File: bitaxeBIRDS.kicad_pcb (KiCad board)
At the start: 6 copper layers, 65 x 112 mm, 219 parts, among them J1 XT30, J2 USB_C_Receptacle_USB2.0, J3 Conn_01x04, J4 Conn_01x04, SW1 SWITCH-SPST, SW2 SWITCH-SPST, U1 TPSM861253RDXR, U10 MCP1824T-1202E/OT, U11 MCP1824T-1202E/OT, U12 MCP1824T-1202E/OT, U13 EMC2103-2, U2 TPS546D24S, U3 TPS546D24S, U4 W25Q16JVUXIQ TR, U5 TPS22919DCKR, U6 RP2040, U7 SK6812, U8 SN74AVC4T774, U9 MCP1824T-1202E/OT, Y1 12MHz, Y2 50MHz

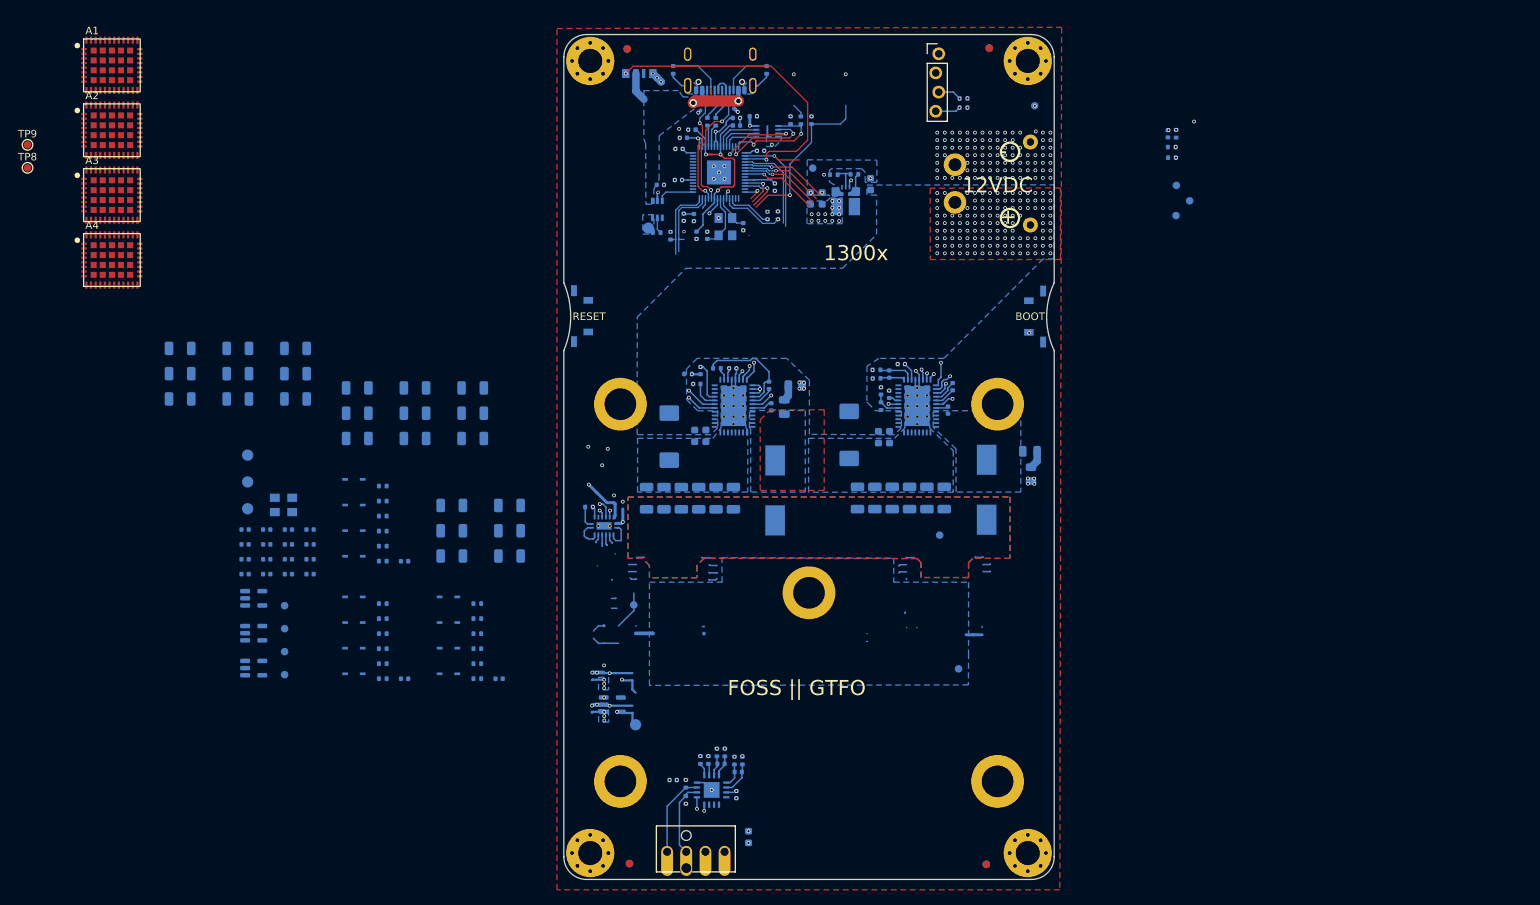
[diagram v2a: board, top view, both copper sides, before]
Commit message: switched to smaller level shifter diodes. switched ASIC modes
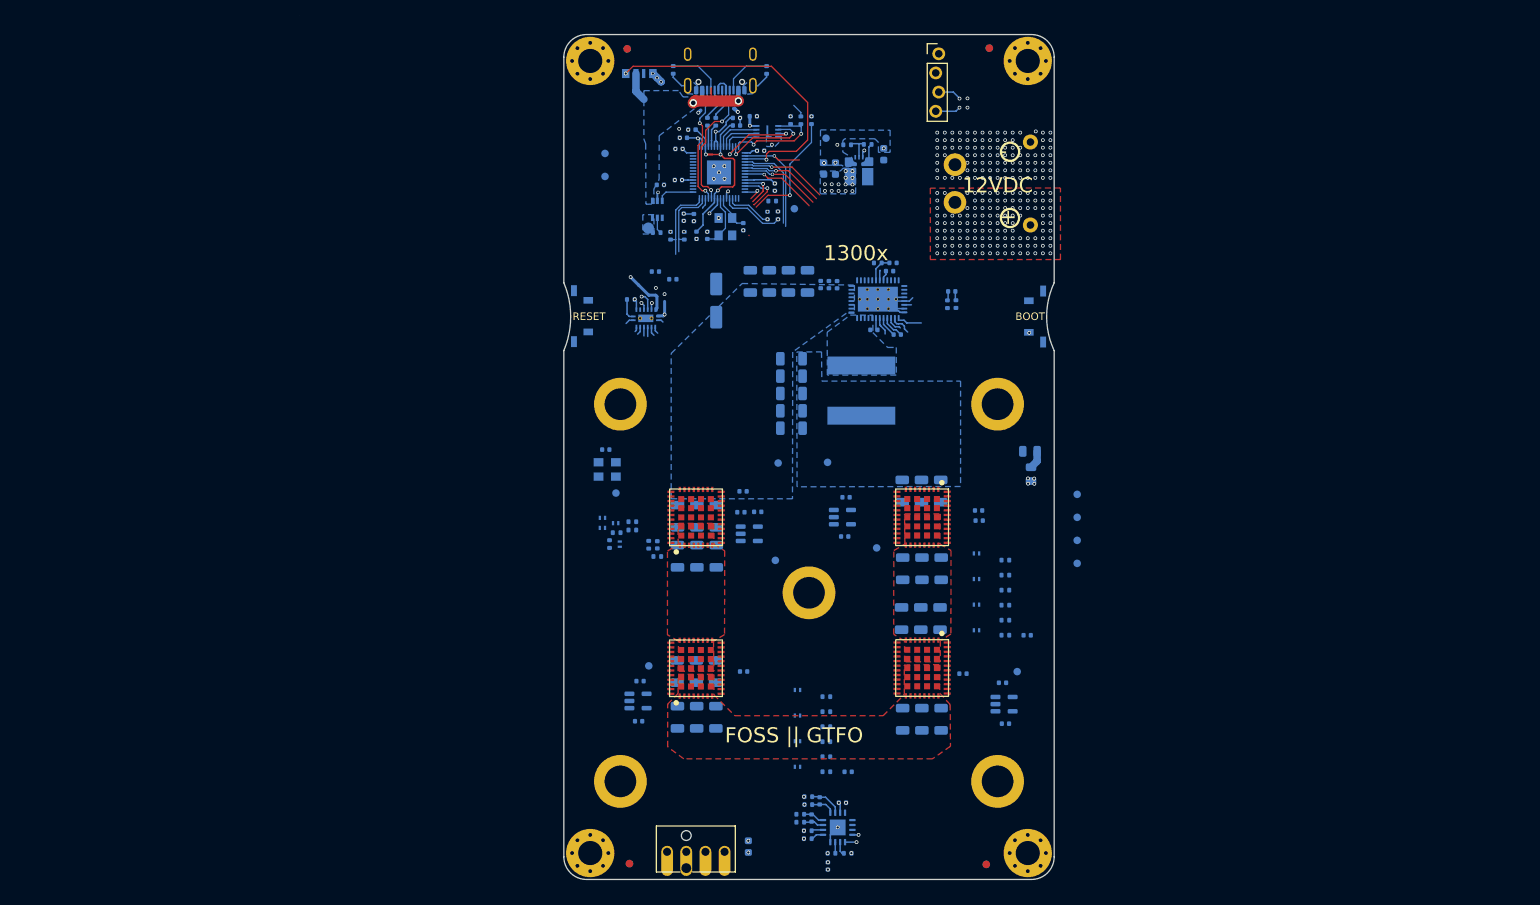
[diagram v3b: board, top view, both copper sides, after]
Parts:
- removed the C10 at (115.8, 91.2)
- removed the C11 at (116.1, 84.3)
- removed the C16 at (116.6, 82.5)
- removed the C22 at (125.7, 84.5)
- removed the C24 at (126.0, 87.3)
- removed C26: 1000pF, Capacitor_SMD:C_0805_2012Metric
- removed C27, C28: 33pF, Capacitor_SMD:C_0402_1005Metric
- removed C29, C30, C32, C36, C38, C40, C41: 100uF, Capacitor_SMD:C_1206_3216Metric
- removed C7: 10uF, Capacitor_SMD:C_0603_1608Metric
- removed the C8 at (117.3, 91.2)
- removed L2: 300nH, bitaxe:SLC1175-271MEC_COC
- removed NT2: NetTie_2, bitaxe:NetTie-2_SMD_Pad0.2mmx1mm
- removed R11: 1, Resistor_SMD:R_0805_2012Metric
- removed R12: 10k, Resistor_SMD:R_0402_1005Metric
- removed the R4 at (151.5, 47.7)
- removed the R6 at (151.5, 46.5)
- removed the R7 at (179.1, 54.3)
- removed R9: 10, Resistor_SMD:R_0402_1005Metric
- removed TP2: SDA, bitaxe:TestPoint_Pad_D1.0mm
- removed TP3: GND, bitaxe:TestPoint_Pad_D1.0mm
- removed TP4: SCL, bitaxe:TestPoint_Pad_D1.0mm
- removed TP5: ALRT, bitaxe:TestPoint_Pad_D1.0mm
- removed U3: TPS546D24S, bitaxe:LQFN40-CLIP
- added C13: 4.7nF, Capacitor_SMD:C_0402_1005Metric, B.Cu at (133.6, 71.2)
- added C14: 2.2nF, Capacitor_SMD:C_0402_1005Metric, B.Cu at (134.7, 71.2)
- added C3: 22uF, Capacitor_SMD:C_1206_3216Metric, B.Cu at (123.2, 70.7)
- added C5: 22uF, Capacitor_SMD:C_1206_3216Metric, B.Cu at (128.3, 70.7)
- added TP1: PWR_EN, bitaxe:TestPoint_Pad_D1.0mm, B.Cu at (129.1, 61.1)
- A1: renamed from A4; value BZM2_MODE1 -> BZM2_MODE0
- A2: renamed from A3; value BZM2_MODE0 -> BZM2_MODE1
- A3: renamed from A2; value BZM2_MODE1 -> BZM2_MODE0
- A4: renamed from A1; value BZM2_MODE0 -> BZM2_MODE1
- C2: renamed from C5; value 33uF -> 27uF; footprint Capacitor_Tantalum_SMD:CP_EIA-7343-31_Kemet-D -> Capacitor_SMD:CP_Elec_5x5.9
- C20: renamed from C31; value 100uF -> 47uF
- C4: value 0.1uF -> 22uF; footprint Capacitor_SMD:C_0402_1005Metric -> Capacitor_SMD:C_1206_3216Metric
- C6: value 33uF -> 22uF; footprint Capacitor_Tantalum_SMD:CP_EIA-7343-31_Kemet-D -> Capacitor_SMD:C_1206_3216Metric
- C9: value 10uF -> 1uF; footprint Capacitor_SMD:C_0603_1608Metric -> Capacitor_SMD:C_0402_1005Metric
- D1, D10, D11, D12, D2, D3, D4, D5, D6, D7, D8, D9: value 1SS380VMTE-17 -> DLLFSD01LPH4-7B; footprint bitaxe:SOD-323FLUMD2_ROM -> bitaxe:DIODE_DLLFSD01LPH4-7B_DIO
- L1: value 300nH -> 1.2uH; footprint bitaxe:SLC1175-271MEC_COC -> bitaxe:XAL1060122MEC
- TP10: footprint TestPoint:TestPoint_Pad_D1.0mm -> bitaxe:TestPoint_Pad_D1.0mm
- TP11: value CLKI -> RX; footprint TestPoint:TestPoint_Pad_D1.0mm -> bitaxe:TestPoint_Pad_D1.0mm
- TP12: value CLKI -> RST; footprint TestPoint:TestPoint_Pad_D1.0mm -> bitaxe:TestPoint_Pad_D1.0mm
- TP13: value CLKI -> TX; footprint TestPoint:TestPoint_Pad_D1.0mm -> bitaxe:TestPoint_Pad_D1.0mm
- TP14: value CLKI -> TRP; footprint TestPoint:TestPoint_Pad_D1.0mm -> bitaxe:TestPoint_Pad_D1.0mm
- TP15, TP16, TP17, TP18: footprint TestPoint:TestPoint_Pad_D1.5mm -> bitaxe:TestPoint_Pad_D1.0mm
- TP8: value TestPoint -> SDA; footprint TestPoint:TestPoint_Pad_D1.0mm -> bitaxe:TestPoint_Pad_D1.0mm; moved to B.Cu
- TP9: value TestPoint -> SCL; footprint TestPoint:TestPoint_Pad_D1.0mm -> bitaxe:TestPoint_Pad_D1.0mm; moved to B.Cu
- U2: value TPS546D24S -> TPS546D24ARVFR
- moved A3 128.9 mm to (146.0, 122.0), turned to -90 degrees
- moved A4 123.0 mm to (146.0, 102.0), turned to -90 degrees
- moved TP11 106.1 mm to (166.6, 108.1), turned to 180 degrees
- moved TP12 106.1 mm to (166.6, 105.0), turned to 180 degrees
- moved TP13 106.1 mm to (166.6, 102.0), turned to 180 degrees
- moved TP14 106.1 mm to (166.6, 99.0), turned to 180 degrees
- moved TP16 105.1 mm to (158.6, 122.5), turned to 180 degrees
- moved C131 101.6 mm to (148.5, 98.5), turned to 90 degrees
- moved U10 99.9 mm to (156.9, 126.8)
- moved A2 99.6 mm to (116.0, 122.0), turned to 90 degrees
- moved C132 99.5 mm to (145.9, 98.5), turned to 90 degrees
- moved C133 97.6 mm to (143.4, 98.5), turned to 90 degrees
- moved C115 97.5 mm to (148.4, 115.4), turned to 90 degrees
- moved C60 97.3 mm to (153.5, 101.1)
- moved C116 96.2 mm to (145.8, 115.4), turned to 90 degrees
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- renumbered C14 to C10, C15 to C11, C3 to C12, C21 to C15, C23 to C16, C25 to C17, C34 to C18, C33 to C21, C35 to C22, C37 to C23, C39 to C24, C2 to C8, R5 to R4, R8 to R5, R10 to R6, R13 to R7, R14 to R8, TP7 to TP19, TP1 to TP6, TP6 to TP7
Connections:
- net /Power/BP1v5_1 renamed /Power/BP1v5
- A1 pad 15: /ASIC/shifter1-2/RX_OUT -> /ASIC/TRIP_1V2
- A1 pad 16: /ASIC/shifter1-2/RESET_OUT -> /ASIC/TX_1V2
- A1 pad 17: /ASIC/shifter1-2/TX_IN -> /ASIC/RST_1V2
- A1 pad 18: /ASIC/shifter1-2/TRIP_IN -> /ASIC/RX_1V2
- A1 pad 31: /ASIC/TRIP_1V2 -> /ASIC/shifter1-2/TRIP_IN
- A1 pad 32: /ASIC/TX_1V2 -> /ASIC/shifter1-2/TX_IN
- A1 pad 33: /ASIC/RST_1V2 -> /ASIC/shifter1-2/RESET_OUT
- A1 pad 34: /ASIC/RX_1V2 -> /ASIC/shifter1-2/RX_OUT
- A1 pad 36: unconnected-(A4-PINSEL-Pad36) -> GND
- A2 pad 15: /ASIC/shifter1-2/TRIP_OUT -> /ASIC/shifter2-3/RX_OUT
- A2 pad 16: /ASIC/shifter1-2/TX_OUT -> /ASIC/shifter2-3/RESET_OUT
- A2 pad 17: /ASIC/shifter1-2/RESET_IN -> /ASIC/shifter2-3/TX_IN
- A2 pad 18: /ASIC/shifter1-2/RX_IN -> /ASIC/shifter2-3/TRIP_IN
- A2 pad 31: /ASIC/shifter2-3/RX_OUT -> /ASIC/shifter1-2/RX_IN
- A2 pad 32: /ASIC/shifter2-3/RESET_OUT -> /ASIC/shifter1-2/RESET_IN
- A2 pad 33: /ASIC/shifter2-3/TX_IN -> /ASIC/shifter1-2/TX_OUT
- A2 pad 34: /ASIC/shifter2-3/TRIP_IN -> /ASIC/shifter1-2/TRIP_OUT
- A2 pad 36: /ASIC/GND1 -> unconnected-(A2-PINSEL-Pad36)
- A3 pad 15: /ASIC/shifter3-4/RX_OUT -> /ASIC/shifter2-3/TRIP_OUT
- A3 pad 16: /ASIC/shifter3-4/RESET_OUT -> /ASIC/shifter2-3/TX_OUT
- A3 pad 17: /ASIC/shifter3-4/TX_IN -> /ASIC/shifter2-3/RESET_IN
- A3 pad 18: /ASIC/shifter3-4/TRIP_IN -> /ASIC/shifter2-3/RX_IN
- A3 pad 31: /ASIC/shifter2-3/TRIP_OUT -> /ASIC/shifter3-4/RX_OUT
- A3 pad 32: /ASIC/shifter2-3/TX_OUT -> /ASIC/shifter3-4/RESET_OUT
- A3 pad 33: /ASIC/shifter2-3/RESET_IN -> /ASIC/shifter3-4/TX_IN
- A3 pad 34: /ASIC/shifter2-3/RX_IN -> /ASIC/shifter3-4/TRIP_IN
- A3 pad 36: unconnected-(A2-PINSEL-Pad36) -> /ASIC/GND2
- A4 pad 15: /ASIC/shifter3-4/TRIP_OUT -> Net-(A4-RX_OUT)
- A4 pad 16: /ASIC/shifter3-4/TX_OUT -> Net-(A4-RESET_OUT)
- A4 pad 17: /ASIC/shifter3-4/RESET_IN -> Net-(A4-TX_IN)
- A4 pad 18: /ASIC/shifter3-4/RX_IN -> Net-(A4-TRIP_IN)
- A4 pad 31: Net-(A1-RX_OUT) -> /ASIC/shifter3-4/TRIP_OUT
- A4 pad 32: Net-(A1-RESET_OUT) -> /ASIC/shifter3-4/TX_OUT
- A4 pad 33: Net-(A1-TX_IN) -> /ASIC/shifter3-4/RESET_IN
- A4 pad 34: Net-(A1-TRIP_IN) -> /ASIC/shifter3-4/RX_IN
- A4 pad 36: /ASIC/GND3 -> unconnected-(A4-PINSEL-Pad36)
- C10 pad 1: /Power/AGND1 -> /Power/AGND
- C4 pad 1: /Power/PWR_EN -> /12V
- NT1 pad 2: /Power/AGND1 -> /Power/AGND
- R7 pad 1: Net-(U2-VOSNS) -> /VDD
- R7 pad 2: /VDD -> Net-(U2-VOSNS)
- R8 pad 1: GND -> Net-(U2-GOSNS)
- R8 pad 2: Net-(U2-GOSNS) -> GND
- TP11 pad 1: Net-(A1-RX_OUT) -> Net-(A4-RX_OUT)
- TP12 pad 1: Net-(A1-RESET_OUT) -> Net-(A4-RESET_OUT)
- TP13 pad 1: Net-(A1-TX_IN) -> Net-(A4-TX_IN)
- TP14 pad 1: Net-(A1-TRIP_IN) -> Net-(A4-TRIP_IN)
- U2 pad 29: unconnected-(U2-MSEL2-Pad29) -> /Power/AGND
- U2 pad 35: /Power/VSHARE -> unconnected-(U2-VSHARE-Pad35)
- U2 pad 37: /Power/AGND1 -> /Power/AGND
- U2 pad 38: /Power/SYNC -> unconnected-(U2-SYNC-Pad38)
- U2 pad 39: /Power/BCX_CLK -> GND
- U2 pad 40: /Power/BCX_DAT -> GND
- U6 pad 2: /Power/PWR_EN -> /Data/PWR_EN
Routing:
- net /ASIC/1V2-1: track 62.7 -> 4.85 mm, vias 2 -> 1
- net /Power/PWR_EN: track 57.8 -> 1.40 mm, vias 3 -> 0
- net GND: track 83.0 -> 29.4 mm, vias 157 -> 141
- net /Data/SCL: track 168.2 -> 116.3 mm, vias 4 -> 3
- net /Data/SDA: track 167.2 -> 118.6 mm, vias 4 -> 3
- net (no net): track 45.7 -> 0.03 mm, vias 6 -> 2
- net /fan/TEMP2_N: track 37.5 -> 0.00 mm
- net /fan/TEMP2_P: track 35.7 -> 0.00 mm
- net /3V3: track 137.9 -> 104.3 mm, vias 39 -> 36
- net /Power/BCX_DAT: track 33.6 -> 0.00 mm, vias 2 -> 0
- net /Power/BCX_CLK: track 31.3 -> 0.00 mm, vias 2 -> 0
- net /5V: track 104.4 -> 74.0 mm, vias 12 -> 4
- net /Power/VSHARE: track 30.1 -> 0.00 mm, vias 2 -> 0
- net /Power/SYNC: track 29.7 -> 0.00 mm, vias 2 -> 0
- net /Power/SMB_ALRT: track 39.9 -> 13.0 mm, vias 1 -> 0
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- added copper zone on F.Cu, net /ASIC/GND1
- added copper zone on F.Cu, net /ASIC/GND2
- added copper zone on F.Cu, net /ASIC/GND3
- removed copper zone on B.Cu, net /12V
- removed copper zone on In2.Cu, net /Power/SW1
- removed copper zone on B.Cu, net /Power/SW2
- removed copper zone on F.Cu, net /Power/SW2
- removed copper zone on In2.Cu, net /Power/SW2
- removed copper zone on F.Cu, net /VDD
- removed copper zone on In2.Cu, net /VDD
- removed copper zone on F.Cu, net GND
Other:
- board text removed: "BAP"

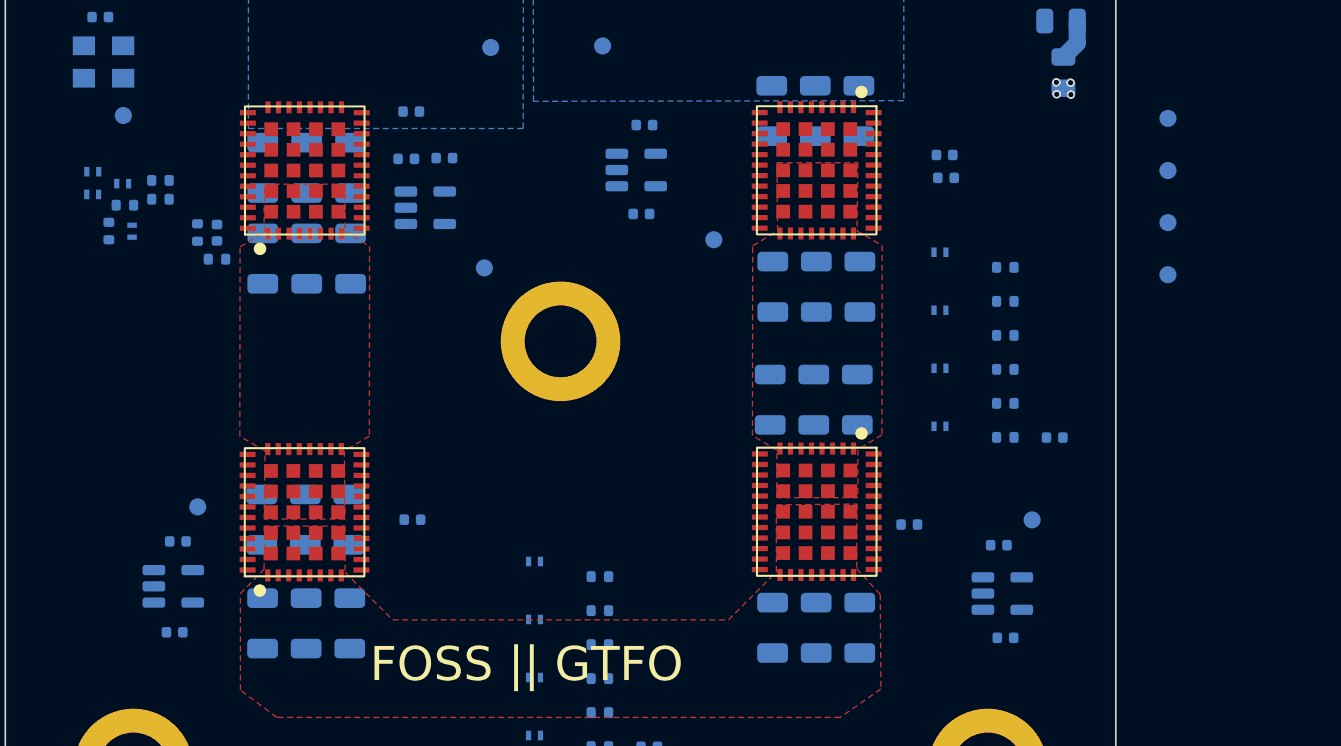
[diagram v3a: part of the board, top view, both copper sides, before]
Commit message: switched to TINY LDOs.
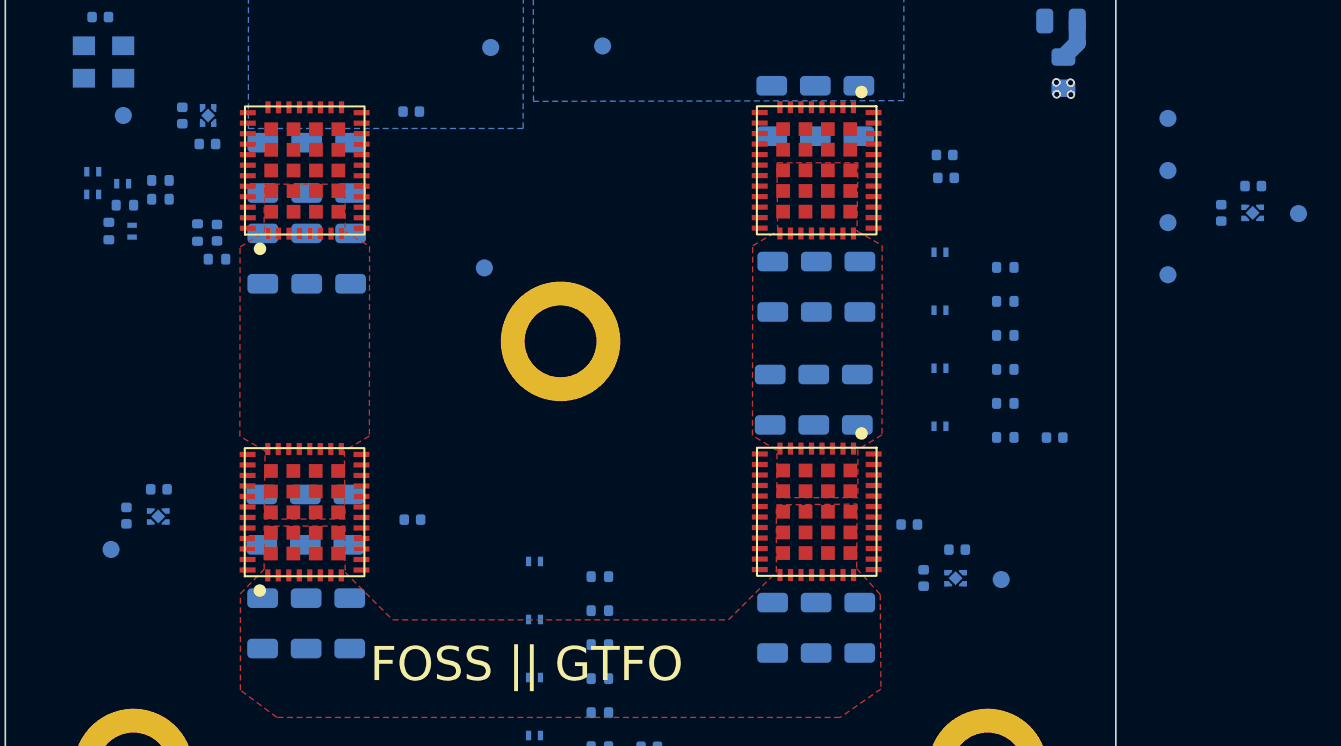
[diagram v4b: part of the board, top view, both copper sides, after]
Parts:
- removed C65, C66, C67, C69, C70, C71: 1uF, Capacitor_SMD:C_0402_1005Metric
- removed TP15: 1V2-4, bitaxe:TestPoint_Pad_D1.0mm
- removed TP16: 1V2-3, bitaxe:TestPoint_Pad_D1.0mm
- removed TP17: 1V2-2, bitaxe:TestPoint_Pad_D1.0mm
- removed U10, U11, U9: MCP1824T-1202E/OT, Package_TO_SOT_SMD:SOT-23-5
- added C19: 1uF, Capacitor_SMD:C_0402_1005Metric, B.Cu at (107.5, 120.7)
- added C25: 1uF, Capacitor_SMD:C_0402_1005Metric, B.Cu at (154.2, 124.2)
- added C26: 1uF, Capacitor_SMD:C_0402_1005Metric, B.Cu at (152.2, 125.8)
- added C27: 1uF, Capacitor_SMD:C_0402_1005Metric, B.Cu at (171.5, 102.9)
- added C28: 1uF, Capacitor_SMD:C_0402_1005Metric, B.Cu at (169.7, 104.5)
- added C7: 1uF, Capacitor_SMD:C_0402_1005Metric, B.Cu at (105.6, 122.2)
- added TP2: 1V2-2, bitaxe:TestPoint_Pad_D1.0mm, B.Cu at (104.7, 124.2)
- added TP3: 1V2-3, bitaxe:TestPoint_Pad_D1.0mm, B.Cu at (156.8, 125.9)
- added TP4: 1V2-4, bitaxe:TestPoint_Pad_D1.0mm, B.Cu at (174.2, 104.5)
- added U14: TLV75512PDQNR, bitaxe:DQN0004A, B.Cu at (154.1, 125.9)
- added U15: TLV75512PDQNR, bitaxe:DQN0004A, B.Cu at (171.5, 104.5)
- added U3: TLV75512PDQNR, bitaxe:DQN0004A, B.Cu at (110.4, 98.8)
- U12: value MCP1824T-1202E/OT -> TLV75512PDQNR; footprint Package_TO_SOT_SMD:SOT-23-5 -> bitaxe:DQN0004A
- moved U12 23.9 mm to (107.5, 122.2)
- moved C72 13.9 mm to (110.3, 100.5)
- moved C68 13.4 mm to (108.9, 98.8), turned to 90 degrees
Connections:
- A1 pad 2: /ASIC/GND1 -> /ASIC/GND2
- A1 pad 3: /ASIC/GND1 -> /ASIC/GND2
- A1 pad 4: /ASIC/GND1 -> /ASIC/GND2
- A1 pad 41: /ASIC/GND1 -> /ASIC/GND2
- A1 pad 42: /ASIC/GND1 -> /ASIC/GND2
- A1 pad 49: /ASIC/GND1 -> /ASIC/GND2
- A1 pad 5: /ASIC/GND1 -> /ASIC/GND2
- A1 pad 50: /ASIC/GND1 -> /ASIC/GND2
- A1 pad 51: /ASIC/GND1 -> /ASIC/GND2
- A1 pad 52: /ASIC/GND1 -> /ASIC/GND2
- A1 pad 59: /ASIC/GND1 -> /ASIC/GND2
- A1 pad 6: /ASIC/GND1 -> /ASIC/GND2
- A1 pad 60: /ASIC/GND1 -> /ASIC/GND2
- A1 pad 7: /ASIC/GND1 -> /ASIC/GND2
- A1 pad 8: /ASIC/GND1 -> /ASIC/GND2
- A2 pad 14: /ASIC/GND1 -> /ASIC/GND2
- A2 pad 2: /ASIC/GND2 -> /ASIC/GND3
- A2 pad 21: /ASIC/GND1 -> /ASIC/GND2
- A2 pad 22: /ASIC/GND1 -> /ASIC/GND2
- A2 pad 23: /ASIC/GND1 -> /ASIC/GND2
- A2 pad 24: /ASIC/GND1 -> /ASIC/GND2
- A2 pad 25: /ASIC/GND1 -> /ASIC/GND2
- A2 pad 26: /ASIC/GND1 -> /ASIC/GND2
- A2 pad 27: /ASIC/GND1 -> /ASIC/GND2
- A2 pad 28: /ASIC/GND1 -> /ASIC/GND2
- A2 pad 3: /ASIC/GND2 -> /ASIC/GND3
- A2 pad 35: /ASIC/GND1 -> /ASIC/GND2
- A2 pad 4: /ASIC/GND2 -> /ASIC/GND3
- A2 pad 41: /ASIC/GND2 -> /ASIC/GND3
- A2 pad 42: /ASIC/GND2 -> /ASIC/GND3
- A2 pad 43: /ASIC/GND1 -> /ASIC/GND2
- A2 pad 44: /ASIC/GND1 -> /ASIC/GND2
- A2 pad 45: /ASIC/GND1 -> /ASIC/GND2
- A2 pad 46: /ASIC/GND1 -> /ASIC/GND2
- A2 pad 47: /ASIC/GND1 -> /ASIC/GND2
- A2 pad 48: /ASIC/GND1 -> /ASIC/GND2
- A2 pad 49: /ASIC/GND2 -> /ASIC/GND3
- A2 pad 5: /ASIC/GND2 -> /ASIC/GND3
- A2 pad 50: /ASIC/GND2 -> /ASIC/GND3
- A2 pad 51: /ASIC/GND2 -> /ASIC/GND3
- A2 pad 52: /ASIC/GND2 -> /ASIC/GND3
- A2 pad 53: /ASIC/GND1 -> /ASIC/GND2
- A2 pad 54: /ASIC/GND1 -> /ASIC/GND2
- A2 pad 55: /ASIC/GND1 -> /ASIC/GND2
- A2 pad 56: /ASIC/GND1 -> /ASIC/GND2
- A2 pad 57: /ASIC/GND1 -> /ASIC/GND2
- A2 pad 58: /ASIC/GND1 -> /ASIC/GND2
- A2 pad 59: /ASIC/GND2 -> /ASIC/GND3
- A2 pad 6: /ASIC/GND2 -> /ASIC/GND3
- A2 pad 60: /ASIC/GND2 -> /ASIC/GND3
- A2 pad 7: /ASIC/GND2 -> /ASIC/GND3
- A2 pad 8: /ASIC/GND2 -> /ASIC/GND3
- A3 pad 14: /ASIC/GND2 -> /ASIC/GND3
- A3 pad 2: /ASIC/GND3 -> /ASIC/GND4
- A3 pad 21: /ASIC/GND2 -> /ASIC/GND3
- A3 pad 22: /ASIC/GND2 -> /ASIC/GND3
- A3 pad 23: /ASIC/GND2 -> /ASIC/GND3
- A3 pad 24: /ASIC/GND2 -> /ASIC/GND3
- A3 pad 25: /ASIC/GND2 -> /ASIC/GND3
- A3 pad 26: /ASIC/GND2 -> /ASIC/GND3
- A3 pad 27: /ASIC/GND2 -> /ASIC/GND3
- A3 pad 28: /ASIC/GND2 -> /ASIC/GND3
- A3 pad 3: /ASIC/GND3 -> /ASIC/GND4
- A3 pad 35: /ASIC/GND2 -> /ASIC/GND3
- A3 pad 4: /ASIC/GND3 -> /ASIC/GND4
- A3 pad 41: /ASIC/GND3 -> /ASIC/GND4
- A3 pad 42: /ASIC/GND3 -> /ASIC/GND4
- A3 pad 43: /ASIC/GND2 -> /ASIC/GND3
- A3 pad 44: /ASIC/GND2 -> /ASIC/GND3
- A3 pad 45: /ASIC/GND2 -> /ASIC/GND3
- A3 pad 46: /ASIC/GND2 -> /ASIC/GND3
- A3 pad 47: /ASIC/GND2 -> /ASIC/GND3
- A3 pad 48: /ASIC/GND2 -> /ASIC/GND3
- A3 pad 49: /ASIC/GND3 -> /ASIC/GND4
- A3 pad 5: /ASIC/GND3 -> /ASIC/GND4
- A3 pad 50: /ASIC/GND3 -> /ASIC/GND4
- A3 pad 51: /ASIC/GND3 -> /ASIC/GND4
- A3 pad 52: /ASIC/GND3 -> /ASIC/GND4
- A3 pad 53: /ASIC/GND2 -> /ASIC/GND3
- A3 pad 54: /ASIC/GND2 -> /ASIC/GND3
- A3 pad 55: /ASIC/GND2 -> /ASIC/GND3
- A3 pad 56: /ASIC/GND2 -> /ASIC/GND3
- A3 pad 57: /ASIC/GND2 -> /ASIC/GND3
- A3 pad 58: /ASIC/GND2 -> /ASIC/GND3
- A3 pad 59: /ASIC/GND3 -> /ASIC/GND4
- A3 pad 6: /ASIC/GND3 -> /ASIC/GND4
- A3 pad 60: /ASIC/GND3 -> /ASIC/GND4
- A3 pad 7: /ASIC/GND3 -> /ASIC/GND4
- A3 pad 8: /ASIC/GND3 -> /ASIC/GND4
- A4 pad 14: /ASIC/GND3 -> /ASIC/GND4
- A4 pad 21: /ASIC/GND3 -> /ASIC/GND4
- A4 pad 22: /ASIC/GND3 -> /ASIC/GND4
- A4 pad 23: /ASIC/GND3 -> /ASIC/GND4
- A4 pad 24: /ASIC/GND3 -> /ASIC/GND4
- A4 pad 25: /ASIC/GND3 -> /ASIC/GND4
- A4 pad 26: /ASIC/GND3 -> /ASIC/GND4
- A4 pad 27: /ASIC/GND3 -> /ASIC/GND4
- A4 pad 28: /ASIC/GND3 -> /ASIC/GND4
- A4 pad 35: /ASIC/GND3 -> /ASIC/GND4
- A4 pad 43: /ASIC/GND3 -> /ASIC/GND4
- A4 pad 44: /ASIC/GND3 -> /ASIC/GND4
- A4 pad 45: /ASIC/GND3 -> /ASIC/GND4
- A4 pad 46: /ASIC/GND3 -> /ASIC/GND4
- A4 pad 47: /ASIC/GND3 -> /ASIC/GND4
- A4 pad 48: /ASIC/GND3 -> /ASIC/GND4
- A4 pad 53: /ASIC/GND3 -> /ASIC/GND4
- A4 pad 54: /ASIC/GND3 -> /ASIC/GND4
- A4 pad 55: /ASIC/GND3 -> /ASIC/GND4
- A4 pad 56: /ASIC/GND3 -> /ASIC/GND4
- A4 pad 57: /ASIC/GND3 -> /ASIC/GND4
- A4 pad 58: /ASIC/GND3 -> /ASIC/GND4
- C100 pad 2: /ASIC/GND2 -> /ASIC/GND3
- C101 pad 2: /ASIC/GND2 -> /ASIC/GND3
- C107 pad 1: /ASIC/GND1 -> /ASIC/GND2
- C108 pad 1: /ASIC/GND1 -> /ASIC/GND2
- C109 pad 1: /ASIC/GND1 -> /ASIC/GND2
- C115 pad 2: /ASIC/GND3 -> /ASIC/GND4
- C116 pad 2: /ASIC/GND3 -> /ASIC/GND4
- C117 pad 2: /ASIC/GND3 -> /ASIC/GND4
- C123 pad 1: /ASIC/GND2 -> /ASIC/GND3
- C124 pad 1: /ASIC/GND2 -> /ASIC/GND3
- C125 pad 1: /ASIC/GND2 -> /ASIC/GND3
- C139 pad 1: /ASIC/GND3 -> /ASIC/GND4
- C140 pad 1: /ASIC/GND3 -> /ASIC/GND4
- C141 pad 1: /ASIC/GND3 -> /ASIC/GND4
- C60 pad 2: /ASIC/GND3 -> /ASIC/GND4
- C61 pad 2: /ASIC/GND3 -> /ASIC/GND4
- C62 pad 2: /ASIC/GND2 -> /ASIC/GND3
- C63 pad 2: /ASIC/GND1 -> /ASIC/GND2
- C83 pad 2: /ASIC/GND1 -> /ASIC/GND2
- C84 pad 2: /ASIC/GND1 -> /ASIC/GND2
- C85 pad 2: /ASIC/GND1 -> /ASIC/GND2
- C99 pad 2: /ASIC/GND2 -> /ASIC/GND3
- R36 pad 1: /ASIC/GND1 -> /ASIC/GND2
- R40 pad 2: /ASIC/GND1 -> /ASIC/GND2
- R41 pad 2: /ASIC/GND1 -> /ASIC/GND2
- R42 pad 1: /ASIC/GND2 -> /ASIC/GND3
- R46 pad 2: /ASIC/GND2 -> /ASIC/GND3
- R47 pad 2: /ASIC/GND2 -> /ASIC/GND3
- R48 pad 1: /ASIC/GND3 -> /ASIC/GND4
- R52 pad 2: /ASIC/GND3 -> /ASIC/GND4
- U12 pad 1: /5V_SWITCH -> /ASIC/1V2-2
- U12 pad 2: GND -> /ASIC/GND2
- U12 pad 4: unconnected-(U12-PG-Pad4) -> /5V_SWITCH
- U12 pad 5: /ASIC/1V2-1 -> /ASIC/GND2
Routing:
- net /Power/AGND: track 8.03 -> 1.30 mm
- removed copper zone on In2.Cu, net /12V
- removed copper zone on F.Cu, net /ASIC/GND1
